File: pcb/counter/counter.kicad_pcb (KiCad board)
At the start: 2 copper layers, 91.4 x 51.8 mm, 17 parts, among them J1 Conn_01x01, J2 Conn_01x01, J3 Conn_01x01, J4 Conn_01x06, J5 Conn_01x02, J6 Conn_01x05, J7 Conn_01x03, Q1 Q_NPN_CBE, U1 74HC08

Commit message: Update.
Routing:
- net Net-(R1-Pad2): track 13.9 -> 14.9 mm
- net Net-(J4-Pad1): track 39.2 -> 39.9 mm
- net GND: track 151.5 -> 150.9 mm
- net +5V: track 130.9 -> 131.4 mm
- net Net-(C1-Pad1): track 32.1 -> 32.6 mm
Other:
- net class Default removed

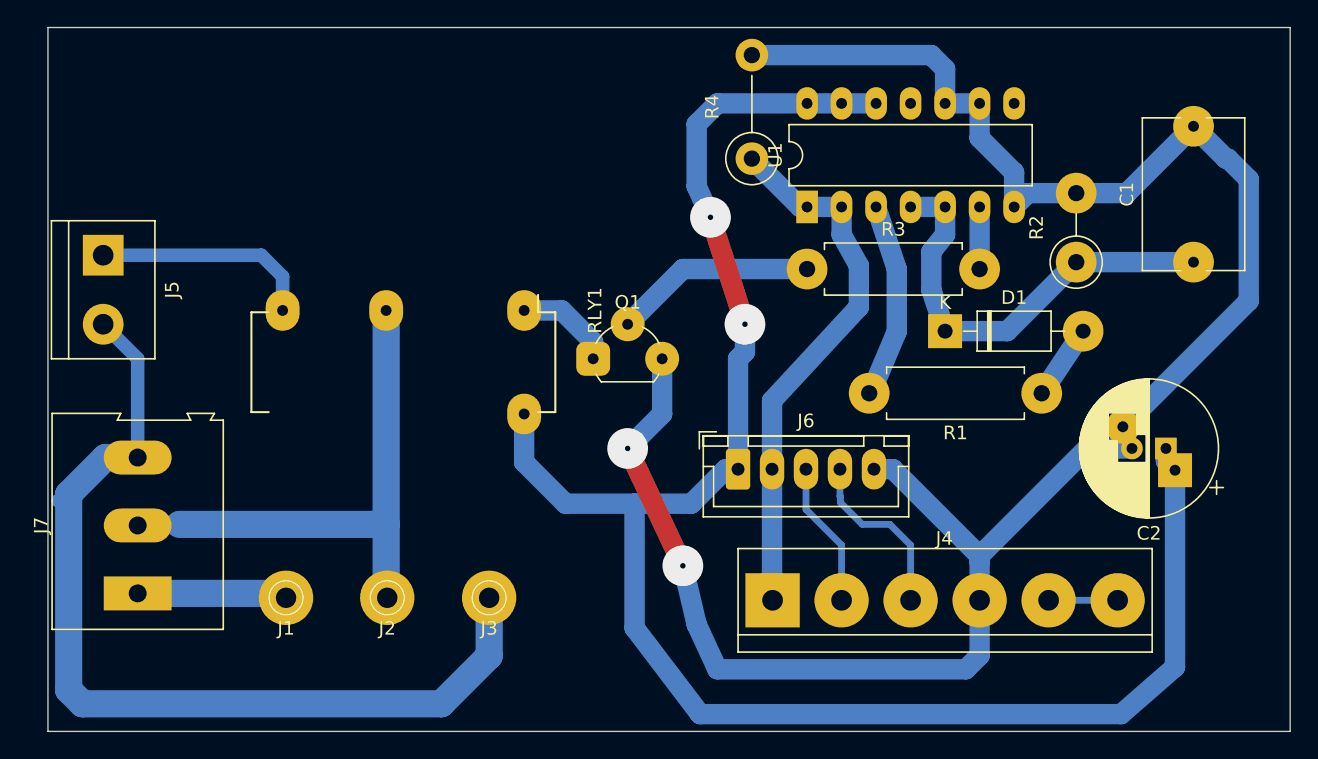
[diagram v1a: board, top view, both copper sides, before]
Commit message: Update footprints for SMD version.
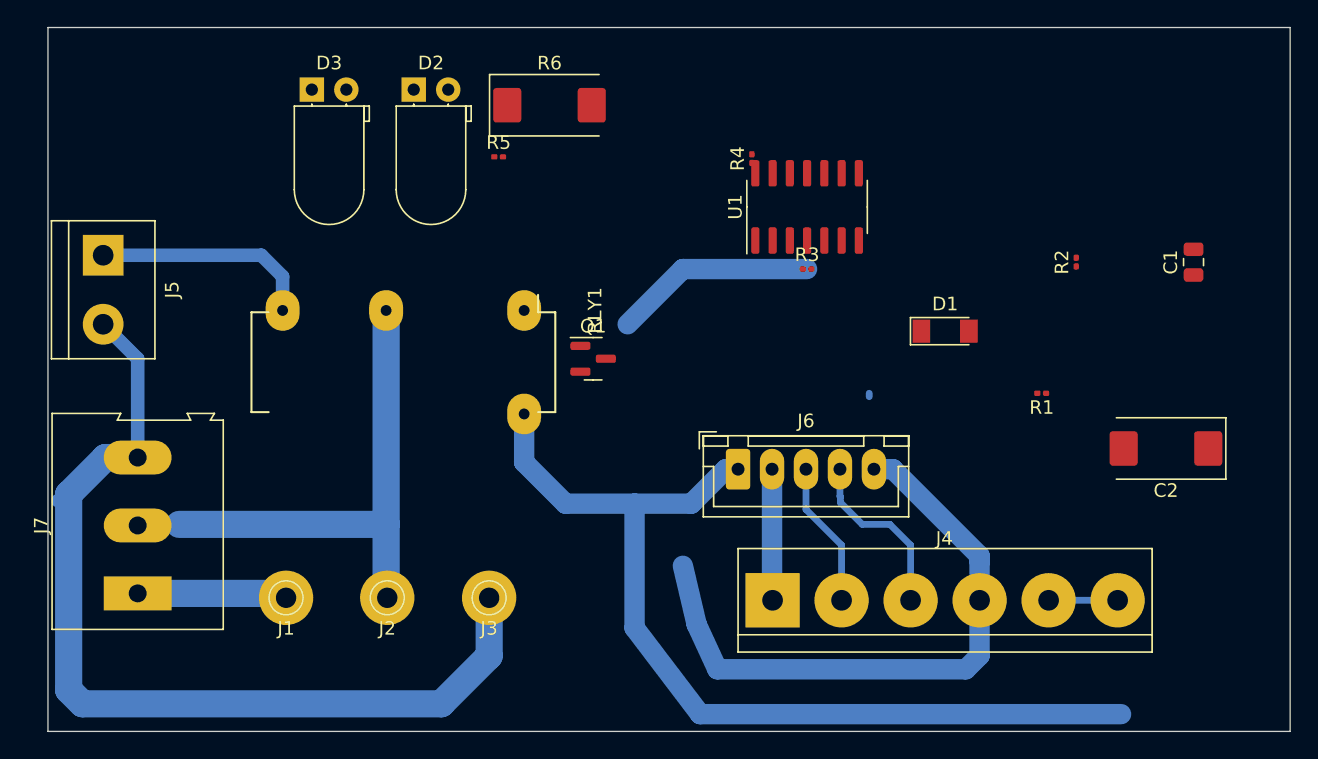
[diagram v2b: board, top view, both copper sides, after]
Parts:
- added D2: LED, LED_THT:LED_D5.0mm_Horizontal_O1.27mm_Z3.0mm, F.Cu at (91.9, 37.6)
- added D3: LED, LED_THT:LED_D5.0mm_Horizontal_O1.27mm_Z3.0mm, F.Cu at (84.4, 37.6)
- added R5: 820, Resistor_SMD:R_0201_0603Metric, F.Cu at (98.2, 42.5)
- added R6: 820, Capacitor_Tantalum_SMD:CP_EIA-7343-40_Kemet-Y, F.Cu at (101.9, 38.7)
- C1: value 1u -> 10u; footprint Capacitor_THT:C_Rect_L11.0mm_W7.3mm_P10.00mm_MKT -> Capacitor_SMD:C_0805_2012Metric
- C2: footprint Capacitor_THT:CP_Radial_D10.0mm_P2.50mm_P5.00mm -> Capacitor_Tantalum_SMD:CP_EIA-7343-40_Kemet-Y
- D1: footprint Diode_THT:D_DO-41_SOD81_P10.16mm_Horizontal -> Diode_SMD:D_MiniMELF
- J4: value Conn_01x06 -> 0.2"
- J5: value Conn_01x02 -> 0.2"
- J6: value Conn_01x05 -> JST XH
- J7: value Conn_01x03 -> 0.2"
- Q1: value Q_NPN_CBE -> MMBT3904; footprint Package_TO_SOT_THT:TO-92L_Wide -> Package_TO_SOT_SMD:SOT-23
- R1, R3: footprint Resistor_THT:R_Axial_DIN0411_L9.9mm_D3.6mm_P12.70mm_Horizontal -> Resistor_SMD:R_0201_0603Metric
- R2: footprint Resistor_THT:R_Axial_DIN0411_L9.9mm_D3.6mm_P5.08mm_Vertical -> Resistor_SMD:R_0201_0603Metric
- R4: footprint Resistor_THT:R_Axial_DIN0411_L9.9mm_D3.6mm_P7.62mm_Vertical -> Resistor_SMD:R_0201_0603Metric
- U1: value 74HC08 -> 74HCT08; footprint Package_DIP:DIP-14_W7.62mm_LongPads -> Package_SO:SOIC-14_3.9x8.7mm_P1.27mm
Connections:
- J4 pad 2: Net-(J4-Pad2) -> TH
- J6 pad 3: Net-(J4-Pad2) -> TH
- Q1 pad 1: RELAY -> Net-(Q1-Pad1)
- Q1 pad 2: Net-(Q1-Pad2) -> GND
- Q1 pad 3: GND -> RELAY
- R3 pad 1: Net-(Q1-Pad2) -> Net-(Q1-Pad1)
- U1 pad 10: GND -> TH
- U1 pad 12: +5V -> Net-(C1-Pad1)
- U1 pad 13: +5V -> Net-(C1-Pad1)
- U1 pad 9: GND -> TH
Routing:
- net GND: track 150.9 -> 45.6 mm, vias 2 -> 0
- net +5V: track 131.4 -> 69.7 mm, vias 2 -> 0
- net Net-(C1-Pad1): track 32.6 -> 0.00 mm
- net Net-(J4-Pad1): track 39.9 -> 9.67 mm
- net Net-(R1-Pad2): track 14.9 -> 0.25 mm
- net TH: track 0.00 -> 10.7 mm
- net Net-(J4-Pad2): track 10.7 -> 0.00 mm
- net RELAY: track 7.29 -> 0.00 mm
- net Net-(D1-Pad2): track 5.49 -> 0.00 mm
- net Net-(R3-Pad2): track 4.57 -> 0.00 mm

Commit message: Add protection diode; work on routing.
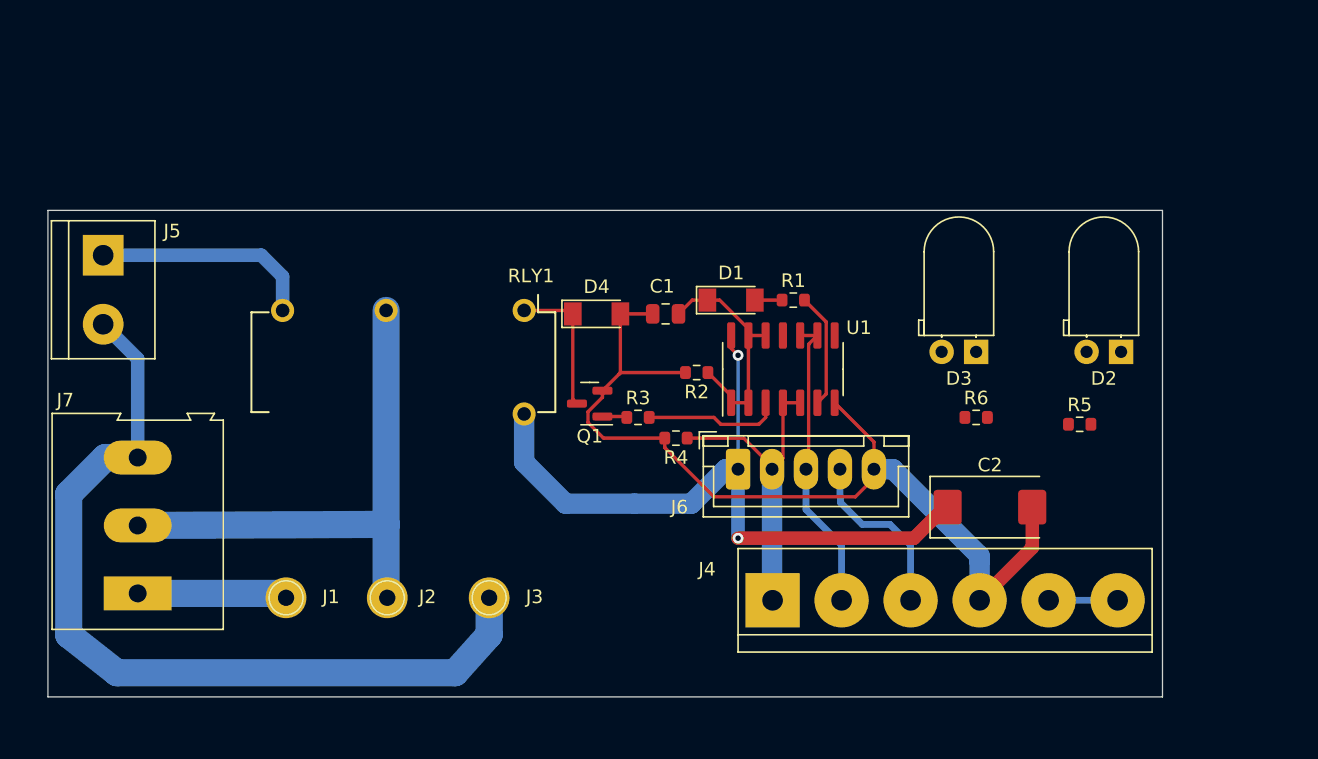
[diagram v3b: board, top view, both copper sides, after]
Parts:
- added D4: 1N4148, Diode_SMD:D_MiniMELF, F.Cu at (105.4, 54.1)
- R1, R2, R3, R4, R5: footprint Resistor_SMD:R_0201_0603Metric -> Resistor_SMD:R_0603_1608Metric
- R6: footprint Capacitor_Tantalum_SMD:CP_EIA-7343-40_Kemet-Y -> Resistor_SMD:R_0603_1608Metric
- moved D2 55.5 mm to (144.0, 56.9), turned to 180 degrees
- moved D3 52.6 mm to (133.3, 56.9), turned to 180 degrees
- moved R5 47.1 mm to (141.0, 62.2)
- moved C1 39.0 mm to (110.5, 54.1), turned to 180 degrees
- moved R6 38.9 mm to (133.3, 61.7)
- moved R2 29.1 mm to (112.8, 58.4), turned to 180 degrees
- moved R4 21.3 mm to (111.3, 63.2), turned to 180 degrees
- moved R1 19.5 mm to (119.9, 53.1), turned to 0 degrees
- moved R3 16.6 mm to (108.5, 61.7)
- moved D1 15.9 mm to (115.3, 53.1)
- moved C2 13.7 mm to (134.4, 68.3), turned to 0 degrees
- moved U1 12.1 mm to (119.1, 58.2)
- moved Q1 3.31 mm to (104.9, 60.7), turned to 180 degrees
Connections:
- U1 pad 1: Net-(J4-Pad1) -> Net-(C1-Pad1)
- U1 pad 2: Net-(J4-Pad1) -> Net-(C1-Pad1)
- U1 pad 3: Net-(R1-Pad2) -> Net-(R3-Pad2)
- U1 pad 4: Net-(C1-Pad1) -> Net-(J4-Pad1)
- U1 pad 5: Net-(C1-Pad1) -> Net-(J4-Pad1)
- U1 pad 6: Net-(R3-Pad2) -> Net-(R1-Pad2)
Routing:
- net GND: track 45.6 -> 69.5 mm
- net Net-(C1-Pad1): track 0.00 -> 17.4 mm
- net +5V: track 69.7 -> 53.1 mm, vias 0 -> 2
- net Net-(Q1-Pad2): track 14.9 -> 0.00 mm
- net Net-(J4-Pad1): track 9.67 -> 23.5 mm
- net TH: track 10.7 -> 22.2 mm
- net RELAY: track 0.00 -> 10.4 mm
- net Net-(R3-Pad2): track 0.00 -> 10.1 mm
- net Net-(R1-Pad2): track 0.25 -> 8.49 mm
- net Net-(J3-Pad1): track 68.6 -> 63.3 mm
- net Net-(Q1-Pad1): track 0.00 -> 1.82 mm
- net Net-(D1-Pad2): track 0.00 -> 1.74 mm
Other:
- board size 91.4 x 51.8 mm -> 82 x 35.8 mm

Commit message: Finish routing.
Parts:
- moved R6 5.84 mm to (127.5, 61.7)
- moved D3 4.83 mm to (133.6, 61.7)
- moved D2 4.83 mm to (144.3, 61.7)
- moved R5 3.09 mm to (137.9, 61.7)
- moved J5 3.05 mm to (69.2, 52.8)
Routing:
- net GND: track 69.5 -> 88.4 mm
- net Net-(R5-Pad1): track 0.00 -> 16.7 mm
- net Net-(R6-Pad1): track 0.00 -> 12.1 mm, vias 0 -> 2
- net Net-(J3-Pad1): track 63.3 -> 60.2 mm
- net Net-(D2-Pad2): track 0.00 -> 2.98 mm
- net Net-(J5-Pad1): track 16.4 -> 13.5 mm
- net Net-(D3-Pad2): track 0.00 -> 2.73 mm
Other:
- board size 82 x 35.8 mm -> 82 x 32.4 mm
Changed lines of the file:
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@@
   )
   (footprint "TerminalBlock:TerminalBlock_bornier-2_P5.08mm" (layer "F.Cu")
-    (at 69.088 49.784 -90)
+    (at 69.215 52.832 -90)
     (descr "simple 2-pin terminal block, pitch 5.08mm, revamped version of bornier2")
     (tags "terminal block bornier2")
@@
   )
   (footprint "Resistor_SMD:R_0603_1608Metric" (layer "F.Cu")
-    (at 140.97 62.23)
+    (at 137.922 61.722)
     (descr "Resistor SMD 0603 (1608 Metric), square (rectangular) end terminal, IPC_7351 nominal, (Body size source: IPC-SM-782 page 72, https://www.pcb-3d.com/wordpress/wp-content/uploads/ipc-sm-782a_amendment_1_and_2.pdf), generated with kicad-footprint-generator")
     (tags "resistor")
@@
   )
   (footprint "LED_THT:LED_D5.0mm_Horizontal_O1.27mm_Z3.0mm" (layer "F.Cu")
-    (at 144.018 56.896 180)
+    (at 144.272 61.722 180)
     (descr "LED, diameter 5.0mm z-position of LED center 3.0mm, 2 pins")
     (tags "LED diameter 5.0mm z-position of LED center 3.0mm 2 pins")
@@
   )
   (footprint "LED_THT:LED_D5.0mm_Horizontal_O1.27mm_Z3.0mm" (layer "F.Cu")
-    (at 133.35 56.896 180)
+    (at 133.604 61.722 180)
     (descr "LED, diameter 5.0mm z-position of LED center 3.0mm, 2 pins")
     (tags "LED diameter 5.0mm z-position of LED center 3.0mm 2 pins")
@@
   )
   (footprint "Resistor_SMD:R_0603_1608Metric" (layer "F.Cu")
-    (at 133.35 61.722)
+    (at 127.508 61.722)
     (descr "Resistor SMD 0603 (1608 Metric), square (rectangular) end terminal, IPC_7351 nominal, (Body size source: IPC-SM-782 page 72, https://www.pcb-3d.com/wordpress/wp-content/uploads/ipc-sm-782a_amendment_1_and_2.pdf), generated with kicad-footprint-generator")
     (tags "resistor")
@@
     )
   )
-  (gr_line (start 65.024 82.296) (end 65.024 46.482) (layer "Edge.Cuts") (width 0.05))
+  (gr_line (start 65.024 82.296) (end 65.024 49.911) (layer "Edge.Cuts") (width 0.05))
   (gr_line (start 147.066 82.296) (end 65.024 82.296) (layer "Edge.Cuts") (width 0.05))
-  (gr_line (start 65.024 46.482) (end 147.066 46.482) (layer "Edge.Cuts") (width 0.05))
-  (gr_line (start 147.066 46.482) (end 147.066 82.296) (layer "Edge.Cuts") (width 0.05))
+  (gr_line (start 65.024 49.911) (end 147.066 49.911) (layer "Edge.Cuts") (width 0.05))
+  (gr_line (start 147.066 49.911) (end 147.066 82.296) (layer "Edge.Cuts") (width 0.05))
   (segment (start 116.586 60.641) (end 116.586 55.691) (width 0.25) (layer "F.Cu") (net 1))
   (segment (start 114.466 53.086) (end 116.586 55.206) (width 0.25) (layer "F.Cu") (net 1))
@@
   (segment (start 137.4785 68.326) (end 137.4785 71.3095) (width 1) (layer "F.Cu") (net 2))
   (segment (start 107.05475 58.54075) (end 105.8395 59.756) (width 0.25) (layer "F.Cu") (net 2))
+  (segment (start 137.668 68.326) (end 137.4785 68.326) (width 0.25) (layer "F.Cu") (net 2))
+  (segment (start 129.794 65.532) (end 125.824 65.532) (width 0.25) (layer "F.Cu") (net 2))
   (segment (start 114.046 67.564) (end 124.46 67.564) (width 0.25) (layer "F.Cu") (net 2))
+  (segment (start 144.272 61.722) (end 137.668 68.326) (width 0.25) (layer "F.Cu") (net 2))
+  (segment (start 133.604 61.722) (end 129.794 65.532) (width 0.25) (layer "F.Cu") (net 2))
   (segment (start 122.936 60.641) (end 125.824 63.529) (width 0.25) (layer "F.Cu") (net 2))
   (segment (start 107.1755 58.42) (end 107.16 58.4355) (width 0.25) (layer "F.Cu") (net 2))
@@
   (segment (start 89.916 53.848) (end 89.916 69.596) (width 2) (layer "B.Cu") (net 6))
   (segment (start 71.628 69.676) (end 89.916 69.596) (width 2) (layer "B.Cu") (net 6))
-  (segment (start 69.088 54.864) (end 71.628 57.404) (width 1) (layer "B.Cu") (net 7))
+  (segment (start 69.215 62.263) (end 71.628 64.676) (width 1) (layer "F.Cu") (net 7))
+  (segment (start 69.215 57.912) (end 69.215 62.263) (width 1) (layer "F.Cu") (net 7))
   (segment (start 70.104 80.518) (end 94.996 80.518) (width 2) (layer "B.Cu") (net 7))
   (segment (start 66.548 77.724) (end 70.104 80.518) (width 2) (layer "B.Cu") (net 7))
   (segment (start 66.548 67.376) (end 66.548 77.724) (width 2) (layer "B.Cu") (net 7))
-  (segment (start 71.628 57.404) (end 71.628 64.676) (width 1) (layer "B.Cu") (net 7))
   (segment (start 97.5 77.724) (end 97.5 75) (width 2) (layer "B.Cu") (net 7))
   (segment (start 71.628 64.676) (end 69.248 64.676) (width 2) (layer "B.Cu") (net 7))
   (segment (start 94.996 80.518) (end 97.5 77.724) (width 2) (layer "B.Cu") (net 7))
   (segment (start 69.248 64.676) (end 66.548 67.376) (width 2) (layer "B.Cu") (net 7))
+  (segment (start 138.747 61.722) (end 141.732 61.722) (width 0.25) (layer "F.Cu") (net 8))
   (segment (start 123.356 67.564) (end 123.356 67.984) (width 0.5) (layer "B.Cu") (net 9))
   (segment (start 127 69.596) (end 128.524 71.12) (width 0.5) (layer "B.Cu") (net 9))
@@
   (segment (start 118.324 75.144) (end 118.364 75.184) (width 1.5) (layer "B.Cu") (net 10))
   (segment (start 138.684 75.184) (end 143.764 75.184) (width 0.5) (layer "B.Cu") (net 11))
-  (segment (start 69.088 49.784) (end 80.732 49.784) (width 1) (layer "B.Cu") (net 12))
-  (segment (start 80.732 49.784) (end 82.296 51.348) (width 1) (layer "B.Cu") (net 12))
-  (segment (start 82.296 51.348) (end 82.296 53.848) (width 1) (layer "B.Cu") (net 12))
+  (segment (start 70.231 53.848) (end 69.215 52.832) (width 1) (layer "F.Cu") (net 12))
+  (segment (start 82.296 53.848) (end 70.231 53.848) (width 1) (layer "F.Cu") (net 12))
   (segment (start 100.076 53.848) (end 103.406 53.848) (width 0.25) (layer "F.Cu") (net 13))
   (segment (start 103.406 53.848) (end 103.66 54.102) (width 0.25) (layer "F.Cu") (net 13))
@@
   (segment (start 117.348 62.23) (end 117.856 61.722) (width 0.25) (layer "F.Cu") (net 15))
   (segment (start 114.554 62.23) (end 117.348 62.23) (width 0.25) (layer "F.Cu") (net 15))
+  (segment (start 128.333 61.722) (end 131.064 61.722) (width 0.25) (layer "F.Cu") (net 16))
   (segment (start 121.666 55.691) (end 121.021 56.336) (width 0.25) (layer "F.Cu") (net 17))
   (segment (start 121.021 65.335) (end 120.824 65.532) (width 0.25) (layer "F.Cu") (net 17))
@@
   (segment (start 105.8395 61.656) (end 107.567 61.656) (width 0.25) (layer "F.Cu") (net 18))
   (segment (start 107.567 61.656) (end 107.633 61.722) (width 0.25) (layer "F.Cu") (net 18))
+  (segment (start 131.066 55.691) (end 122.936 55.691) (width 0.25) (layer "F.Cu") (net 19))
+  (segment (start 137.097 61.722) (end 131.066 55.691) (width 0.25) (layer "F.Cu") (net 19))
+  (segment (start 126.683 61.722) (end 126.683 60.008) (width 0.25) (layer "F.Cu") (net 20))
+  (segment (start 119.888 58.293) (end 119.126 57.531) (width 0.25) (layer "F.Cu") (net 20))
+  (segment (start 126.683 60.008) (end 124.968 58.293) (width 0.25) (layer "F.Cu") (net 20))
+  (segment (start 119.126 57.531) (end 119.126 55.691) (width 0.25) (layer "F.Cu") (net 20))
+  (via (at 124.968 58.293) (size 0.8) (drill 0.4) (layers "F.Cu" "B.Cu") (net 20))
+  (via (at 119.888 58.293) (size 0.8) (drill 0.4) (layers "F.Cu" "B.Cu") (net 20))
+  (segment (start 124.968 58.293) (end 119.888 58.293) (width 0.25) (layer "B.Cu") (net 20))
 )
